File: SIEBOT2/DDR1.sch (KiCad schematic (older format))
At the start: 19 parts, among them U5 MT46V32M16TG, U6 M25P32

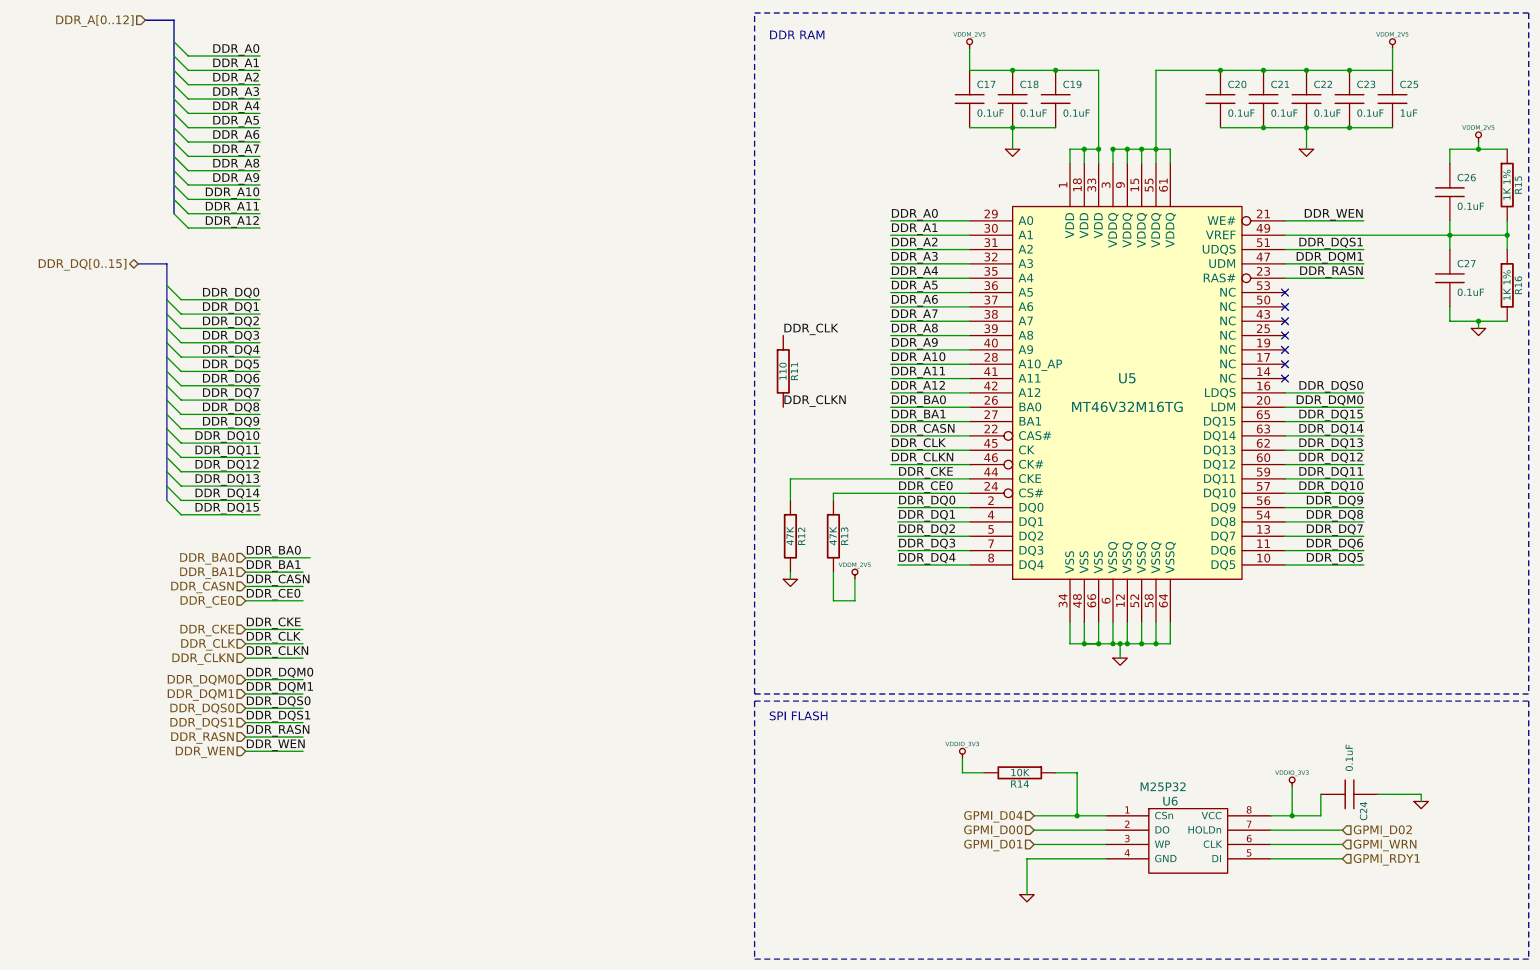
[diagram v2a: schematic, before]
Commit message: STM32 connection fixes + various fixes
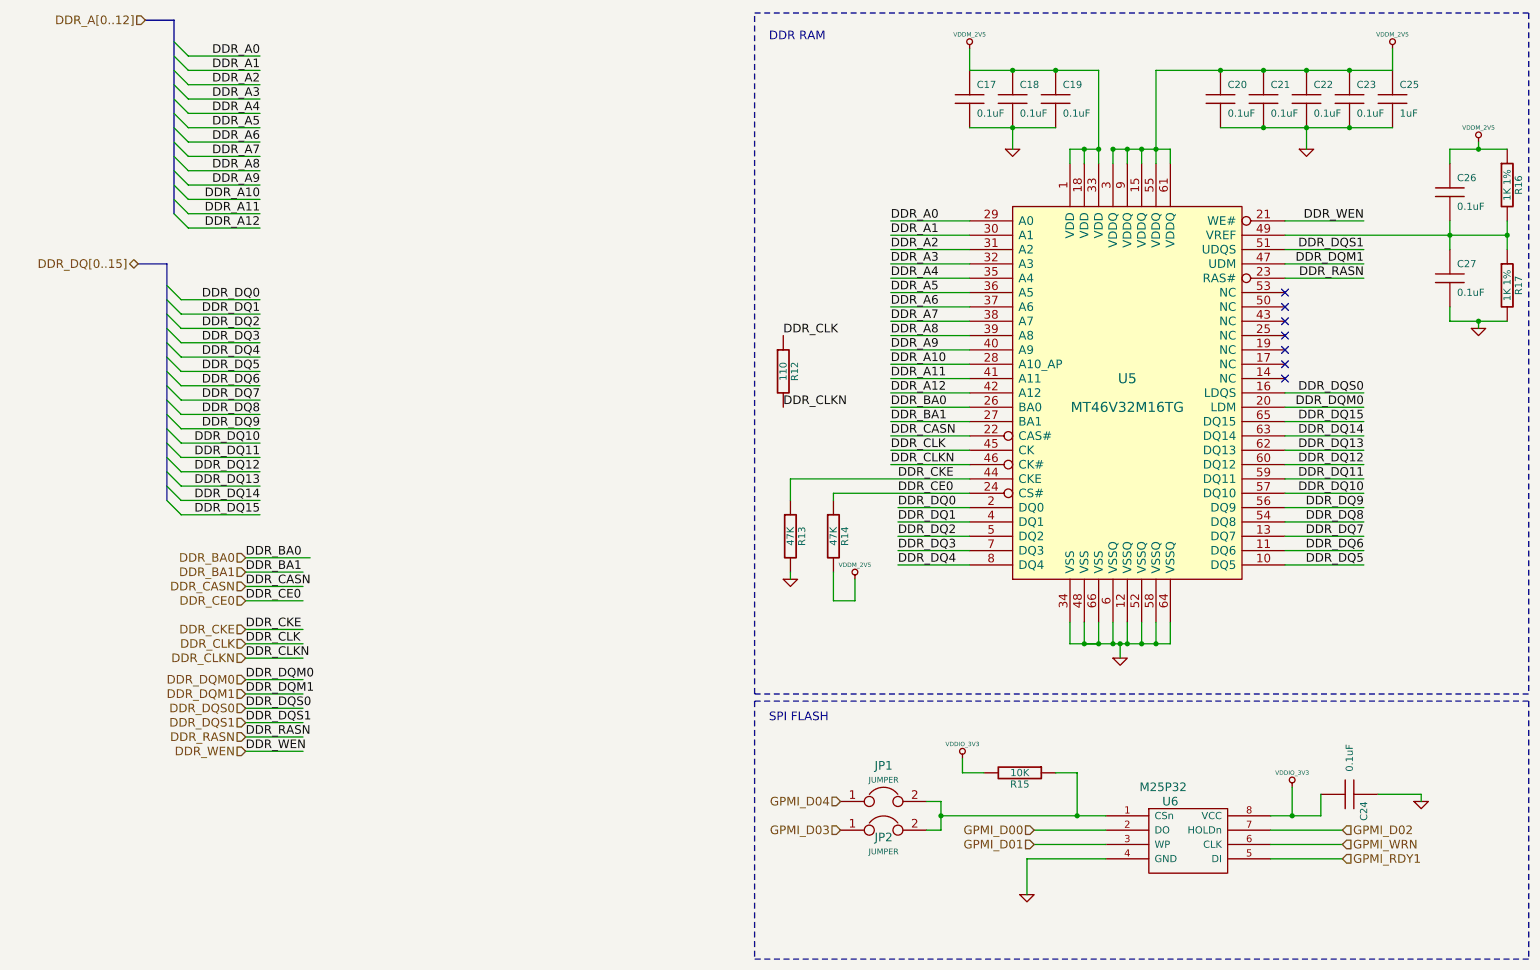
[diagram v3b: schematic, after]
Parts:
- added JP1, JP2: JUMPER, symbol JUMPER
- renumbered R11 to R12, R12 to R13, R13 to R14, R14 to R15, R15 to R16, R16 to R17
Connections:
- net labels added: GPMI_D03
- wire segments 145 -> 148
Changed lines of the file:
@@
-EESchema Schematic File Version 2  date lun 11 abr 2011 13:13:06 COT
+EESchema Schematic File Version 2  date mar 19 abr 2011 23:27:38 COT
+LIBS:mpc17529
 LIBS:dc-dc
 LIBS:stm32f100vxx
@@
 EELAYER END
 $Descr A4 11700 8267
-Sheet 5 6
+Sheet 6 6
 Title ""
-Date "11 apr 2011"
+Date "20 apr 2011"
 Rev ""
 Comp ""
@@
 Comment4 ""
 $EndDescr
+Connection ~ 7050 6150
+Wire Wire Line
+	7050 6150 8200 6150
 Wire Wire Line
 	7700 6250 8200 6250
@@
 Wire Wire Line
 	7700 6350 8200 6350
-Wire Wire Line
-	7700 6150 8200 6150
 Connection ~ 8550 1500
 Connection ~ 8350 1500
@@
 Wire Wire Line
 	9850 6350 9350 6350
-$Comp
-L VDDIO_3V3 #PWR049
+Wire Wire Line
+	6950 6050 7050 6050
+Wire Wire Line
+	7050 6050 7050 6250
+Wire Wire Line
+	7050 6250 6950 6250
+$Comp
+L JUMPER JP2
+U 1 1 4DAE2ED5
+P 6650 6250
+F 0 "JP2" H 6650 6200 60  0000 C CNN
+F 1 "JUMPER" H 6650 6100 40  0000 C CNN
+	1    6650 6250
+	1    0    0    -1
+$EndComp
+$Comp
+L JUMPER JP1
+U 1 1 4DAE2EC1
+P 6650 6050
+F 0 "JP1" H 6650 6300 60  0000 C CNN
+F 1 "JUMPER" H 6650 6200 40  0000 C CNN
+	1    6650 6050
+	1    0    0    -1
+$EndComp
+Text HLabel 6350 6250 0    60   Input ~ 0
+GPMI_D03
+$Comp
+L VDDIO_3V3 #PWR051
 U 1 1 4D7D59A9
 P 7200 5750
-F 0 "#PWR049" H 7200 5850 30  0001 C CNN
+F 0 "#PWR051" H 7200 5850 30  0001 C CNN
 F 1 "VDDIO_3V3" H 7200 5850 30  0000 C CNN
 	1    7200 5750
@@
 $EndComp
 $Comp
-L R R14
+L R R15
 U 1 1 4D7D5980
 P 7600 5850
-F 0 "R14" V 7680 5850 50  0000 C CNN
+F 0 "R15" V 7680 5850 50  0000 C CNN
 F 1 "10K" V 7600 5850 50  0000 C CNN
 	1    7600 5850
@@
 $EndComp
 $Comp
-L VDDM_2V5 #PWR050
+L VDDM_2V5 #PWR052
 U 1 1 4D7D4B15
 P 6450 4500
-F 0 "#PWR050" H 6450 4600 30  0001 C CNN
+F 0 "#PWR052" H 6450 4600 30  0001 C CNN
 F 1 "VDDM_2V5" H 6450 4600 30  0000 C CNN
 	1    6450 4500
@@
 $EndComp
 $Comp
-L R R13
+L R R14
 U 1 1 4D7D4AD6
 P 6300 4200
-F 0 "R13" V 6380 4200 50  0000 C CNN
+F 0 "R14" V 6380 4200 50  0000 C CNN
 F 1 "47K" V 6300 4200 50  0000 C CNN
 	1    6300 4200
@@
 DDR_CLK
 $Comp
-L R R11
+L R R12
 U 1 1 4D41DFB8
 P 5950 3050
-F 0 "R11" V 6030 3050 50  0000 C CNN
+F 0 "R12" V 6030 3050 50  0000 C CNN
 F 1 "110" V 5950 3050 50  0000 C CNN
 	1    5950 3050
@@
 DDR_CASN
 $Comp
-L R R12
+L R R13
 U 1 1 4D418363
 P 6000 4200
-F 0 "R12" V 6080 4200 50  0000 C CNN
+F 0 "R13" V 6080 4200 50  0000 C CNN
 F 1 "47K" V 6000 4200 50  0000 C CNN
 	1    6000 4200
@@
 $EndComp
 $Comp
-L GND #PWR051
+L GND #PWR053
 U 1 1 4D418353
 P 6000 4500
-F 0 "#PWR051" H 6000 4500 30  0001 C CNN
+F 0 "#PWR053" H 6000 4500 30  0001 C CNN
 F 1 "GND" H 6000 4430 30  0001 C CNN
 	1    6000 4500
@@
 DDR_CKE
 $Comp
-L GND #PWR052
+L GND #PWR054
 U 1 1 4D417AF1
 P 10800 2750
-F 0 "#PWR052" H 10800 2750 30  0001 C CNN
+F 0 "#PWR054" H 10800 2750 30  0001 C CNN
 F 1 "GND" H 10800 2680 30  0001 C CNN
 	1    10800 2750
@@
 $EndComp
 $Comp
-L VDDM_2V5 #PWR053
+L VDDM_2V5 #PWR055
 U 1 1 4D417ACD
 P 10800 1450
-F 0 "#PWR053" H 10800 1550 30  0001 C CNN
+F 0 "#PWR055" H 10800 1550 30  0001 C CNN
 F 1 "VDDM_2V5" H 10800 1550 30  0000 C CNN
 	1    10800 1450
@@
 $EndComp
 $Comp
-L R R16
+L R R17
 U 1 1 4D417AA2
 P 11000 2450
-F 0 "R16" V 11080 2450 50  0000 C CNN
+F 0 "R17" V 11080 2450 50  0000 C CNN
 F 1 "1K 1%" V 11000 2450 50  0000 C CNN
 	1    11000 2450
@@
 $EndComp
 $Comp
-L R R15
+L R R16
 U 1 1 4D417A9C
 P 11000 1750
-F 0 "R15" V 11080 1750 50  0000 C CNN
+F 0 "R16" V 11080 1750 50  0000 C CNN
 F 1 "1K 1%" V 11000 1750 50  0000 C CNN
 	1    11000 1750
@@
 $EndComp
 $Comp
-L VDDM_2V5 #PWR054
+L VDDM_2V5 #PWR056
 U 1 1 4D4179A4
 P 7250 800
-F 0 "#PWR054" H 7250 900 30  0001 C CNN
+F 0 "#PWR056" H 7250 900 30  0001 C CNN
 F 1 "VDDM_2V5" H 7250 900 30  0000 C CNN
 	1    7250 800
@@
 $EndComp
 $Comp
-L VDDM_2V5 #PWR055
+L VDDM_2V5 #PWR057
 U 1 1 4D417999
 P 10200 800
-F 0 "#PWR055" H 10200 900 30  0001 C CNN
+F 0 "#PWR057" H 10200 900 30  0001 C CNN
 F 1 "VDDM_2V5" H 10200 900 30  0000 C CNN
 	1    10200 800
@@
 $EndComp
 $Comp
-L GND #PWR056
+L GND #PWR058
 U 1 1 4D41792B
 P 7550 1500
-F 0 "#PWR056" H 7550 1500 30  0001 C CNN
+F 0 "#PWR058" H 7550 1500 30  0001 C CNN
 F 1 "GND" H 7550 1430 30  0001 C CNN
 	1    7550 1500
@@
 $EndComp
 $Comp
-L GND #PWR057
+L GND #PWR059
 U 1 1 4D417882
 P 9600 1500
-F 0 "#PWR057" H 9600 1500 30  0001 C CNN
+F 0 "#PWR059" H 9600 1500 30  0001 C CNN
 F 1 "GND" H 9600 1430 30  0001 C CNN
 	1    9600 1500
@@
 Text HLabel 7700 6250 0    60   Input ~ 0
 GPMI_D00
-Text HLabel 7700 6150 0    60   Input ~ 0
+Text HLabel 6350 6050 0    60   Input ~ 0
 GPMI_D04
 $Comp
-L GND #PWR058
+L GND #PWR060
 U 1 1 4D409664
 P 10400 6050
-F 0 "#PWR058" H 10400 6050 30  0001 C CNN
+F 0 "#PWR060" H 10400 6050 30  0001 C CNN
 F 1 "GND" H 10400 5980 30  0001 C CNN
 	1    10400 6050
@@
 $EndComp
 $Comp
-L VDDIO_3V3 #PWR059
+L VDDIO_3V3 #PWR061
 U 1 1 4D409635
 P 9500 5950
-F 0 "#PWR059" H 9500 6050 30  0001 C CNN
+F 0 "#PWR061" H 9500 6050 30  0001 C CNN
 F 1 "VDDIO_3V3" H 9500 6050 30  0000 C CNN
 	1    9500 5950
@@
 $EndComp
 $Comp
-L GND #PWR060
+L GND #PWR062
 U 1 1 4D409619
 P 7650 6700
-F 0 "#PWR060" H 7650 6700 30  0001 C CNN
+F 0 "#PWR062" H 7650 6700 30  0001 C CNN
 F 1 "GND" H 7650 6630 30  0001 C CNN
 	1    7650 6700
@@
 DDR_WEN
 $Comp
-L GND #PWR061
+L GND #PWR063
 U 1 1 4D319D50
 P 8300 5050
-F 0 "#PWR061" H 8300 5050 30  0001 C CNN
+F 0 "#PWR063" H 8300 5050 30  0001 C CNN
 F 1 "GND" H 8300 4980 30  0001 C CNN
 	1    8300 5050
